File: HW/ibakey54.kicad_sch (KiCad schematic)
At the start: 2 parts, among them U1 Nice!Nano

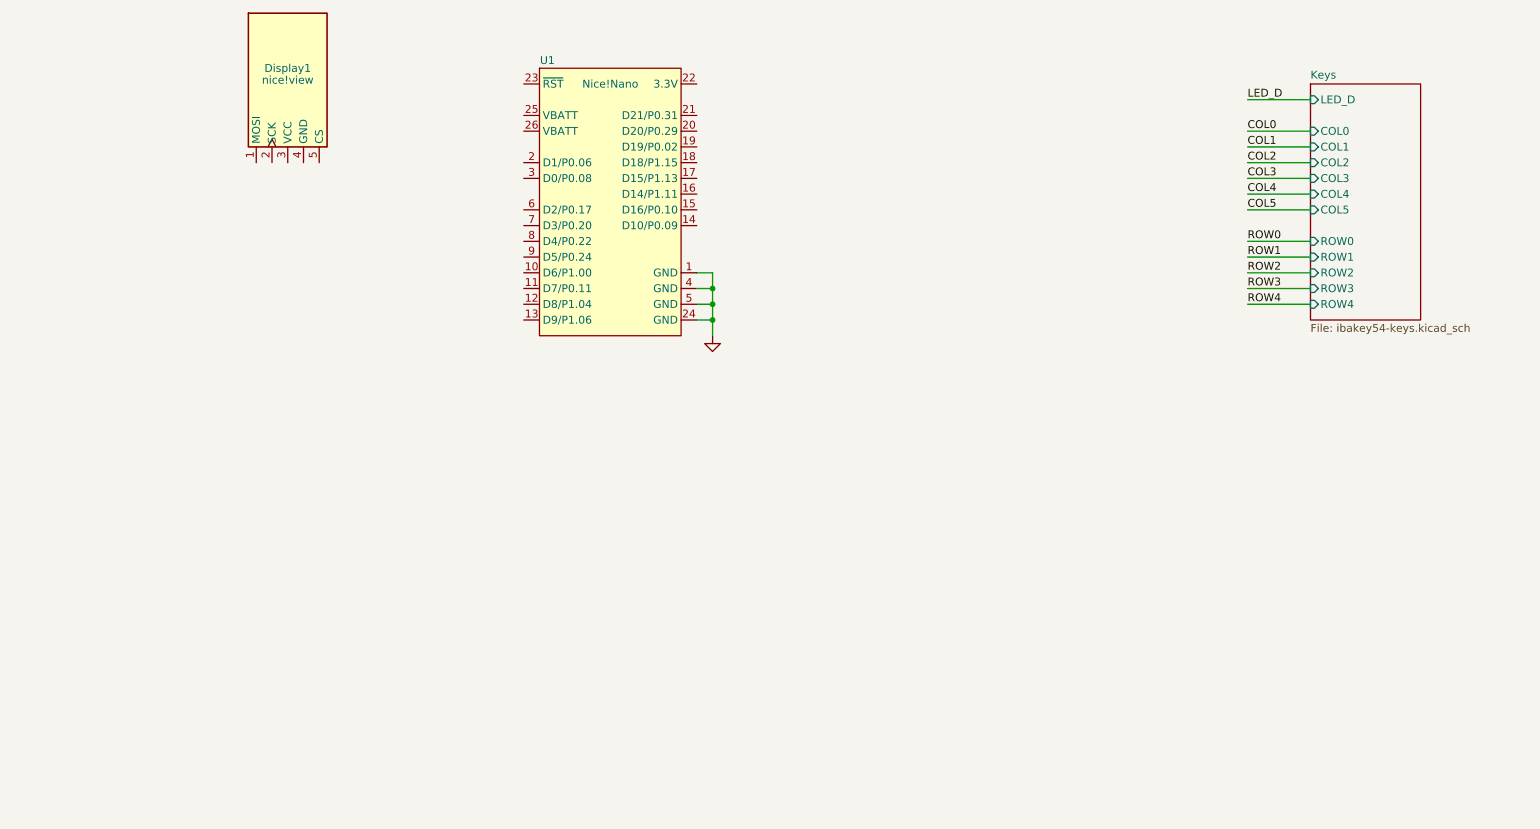
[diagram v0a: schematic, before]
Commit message: finishing main placement & board shape
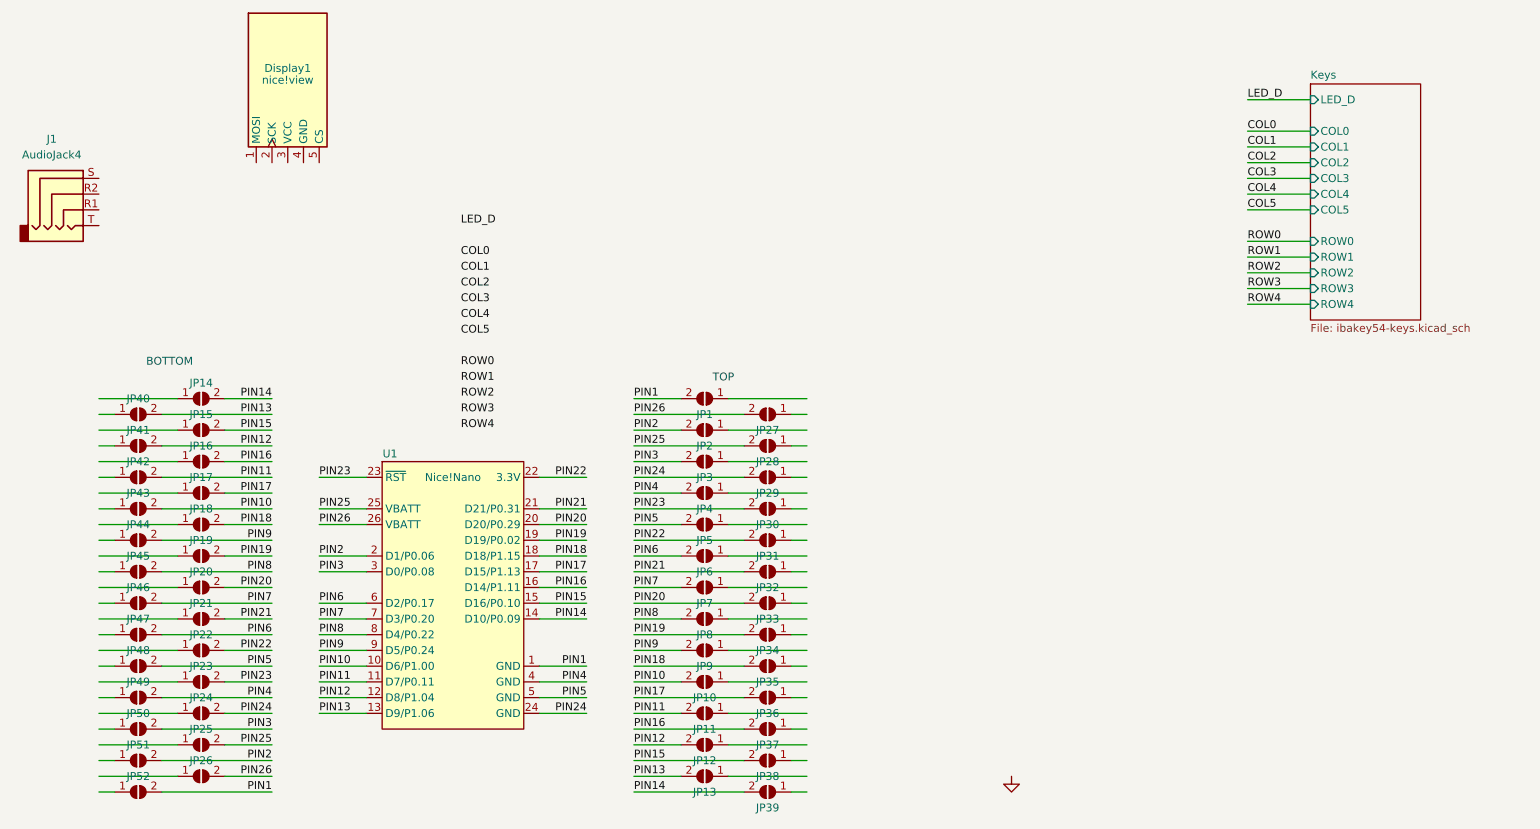
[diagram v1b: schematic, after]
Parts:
- added J1: AudioJack4, CONN-THT-JACK:PJ-320A, symbol Connector_Audio:AudioJack4
- added JP1, JP10, JP11, JP12, JP13, JP14, JP15, JP16, JP17, JP18, JP19, JP2, JP20, JP21, JP22, JP23, JP24, JP25, JP26, JP27, JP28, JP29, JP3, JP30, JP31, JP32, JP33, JP34, JP35, JP36, JP37, JP38, JP39, JP4, JP40, JP41, JP42, JP43, JP44, JP45, JP46, JP47, JP48, JP49, JP5, JP50, JP51, JP52, JP6, JP7, JP8, JP9: SolderJumper_2_Open, Jumper:SolderJumper-2_P1.3mm_Open_TrianglePad1.0x1.5mm, symbol Jumper:SolderJumper_2_Open
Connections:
- net GND: no longer U1.1 (GND), U1.24 (GND), U1.4 (GND), U1.5 (GND)
- net PIN10: now reaches U1.10 (D6/P1.00)
- net PIN10: now also JP10.2 (B), JP43.2 (B)
- net PIN11: now reaches U1.11 (D7/P0.11)
- net PIN11: now also JP11.2 (B), JP42.2 (B)
- net PIN12: now reaches U1.12 (D8/P1.04)
- net PIN12: now also JP12.2 (B), JP41.2 (B)
- net PIN13: now reaches U1.13 (D9/P1.06)
- net PIN13: now also JP13.2 (B), JP40.2 (B)
- net PIN14: now reaches U1.14 (D10/P0.09)
- net PIN14: now also JP14.2 (B), JP39.2 (B)
- net PIN15: now reaches U1.15 (D16/P0.10)
- net PIN15: now also JP15.2 (B), JP38.2 (B)
- net PIN16: now reaches U1.16 (D14/P1.11)
- net PIN16: now also JP16.2 (B), JP37.2 (B)
- net PIN17: now reaches U1.17 (D15/P1.13)
- net PIN17: now also JP17.2 (B), JP36.2 (B)
- net PIN18: now reaches U1.18 (D18/P1.15)
- net PIN18: now also JP18.2 (B), JP35.2 (B)
- net PIN19: now reaches U1.19 (D19/P0.02)
- net PIN19: now also JP19.2 (B), JP34.2 (B)
- net PIN2: now reaches U1.2 (D1/P0.06)
- net PIN2: now also JP2.2 (B), JP51.2 (B)
- net PIN20: now reaches U1.20 (D20/P0.29)
- net PIN20: now also JP20.2 (B), JP33.2 (B)
- net PIN21: now reaches U1.21 (D21/P0.31)
- net PIN21: now also JP21.2 (B), JP32.2 (B)
- net PIN22: now reaches U1.22 (3.3V)
- net PIN22: now also JP22.2 (B), JP31.2 (B)
- net PIN23: now reaches U1.23 (~{RST})
- net PIN23: now also JP23.2 (B), JP30.2 (B)
- net PIN25: now reaches U1.25 (VBATT)
- net PIN25: now also JP25.2 (B), JP28.2 (B)
- net PIN26: now reaches U1.26 (VBATT)
- net PIN26: now also JP26.2 (B), JP27.2 (B)
- net PIN3: now reaches U1.3 (D0/P0.08)
- net PIN3: now also JP3.2 (B), JP50.2 (B)
- net PIN6: now reaches U1.6 (D2/P0.17)
- net PIN6: now also JP47.2 (B), JP6.2 (B)
- net PIN7: now reaches U1.7 (D3/P0.20)
- net PIN7: now also JP46.2 (B), JP7.2 (B)
- net PIN8: now reaches U1.8 (D4/P0.22)
- net PIN8: now also JP45.2 (B), JP8.2 (B)
- net PIN9: now reaches U1.9 (D5/P0.24)
- net PIN9: now also JP44.2 (B), JP9.2 (B)
- new net PIN1: JP1.2 (B), JP52.2 (B), U1.1 (GND)
- new net PIN24: JP24.2 (B), JP29.2 (B), U1.24 (GND)
- new net PIN4: JP4.2 (B), JP49.2 (B), U1.4 (GND)
- new net PIN5: JP48.2 (B), JP5.2 (B), U1.5 (GND)
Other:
- note added: "BOTTOM"
- note added: "TOP"
- moved on the sheet: U1
